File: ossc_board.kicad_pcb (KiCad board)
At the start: 2 copper layers, 124.6 x 68.7 mm, 230 parts, among them J1 VGA, J2 3XRCA_CONN, J3 SCART-F, J4 HDMI_CONN, J5 5VDC_IN, J6 SJ1-3533NG, J7 SJ1-3533NG, P1 JTAG_CONN, P3 mSD_CONN, Q1 BC847, Q2 BC857, SW1 SPST, SW2 SW_PUSH, SW3 SW_PUSH, SW4 DPDT, U1 TVP7002PZP, U10 S25FL216K, U11 IRM-V538/TR1, U12 TLV70012, U13 TLV70025, U14 TLV70012, U15 TLV70018, U16 TLV70018, U17 THS7353, U2 EP4CE15E22, U3 IT6613, U4 SN74LVC2G17, U5 AP7361C, U6 TLV70033, U7 NCP703SN19T1G, U8 PCM1862, U9 TLV70019, Y1 ACHL-27MHZ-EK, Y2 24.576MHz

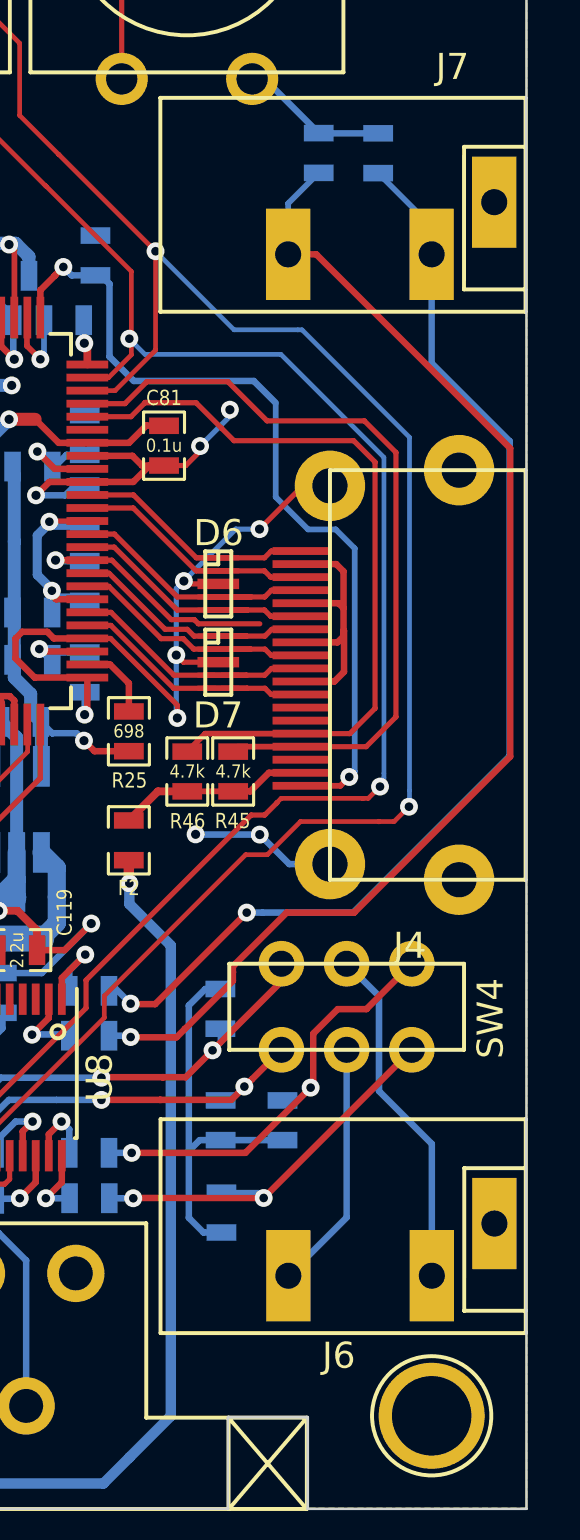
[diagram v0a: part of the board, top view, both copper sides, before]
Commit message: Changed footprint of headphone jack to circular drill
Also, verified DRC rules pass for OSHPark
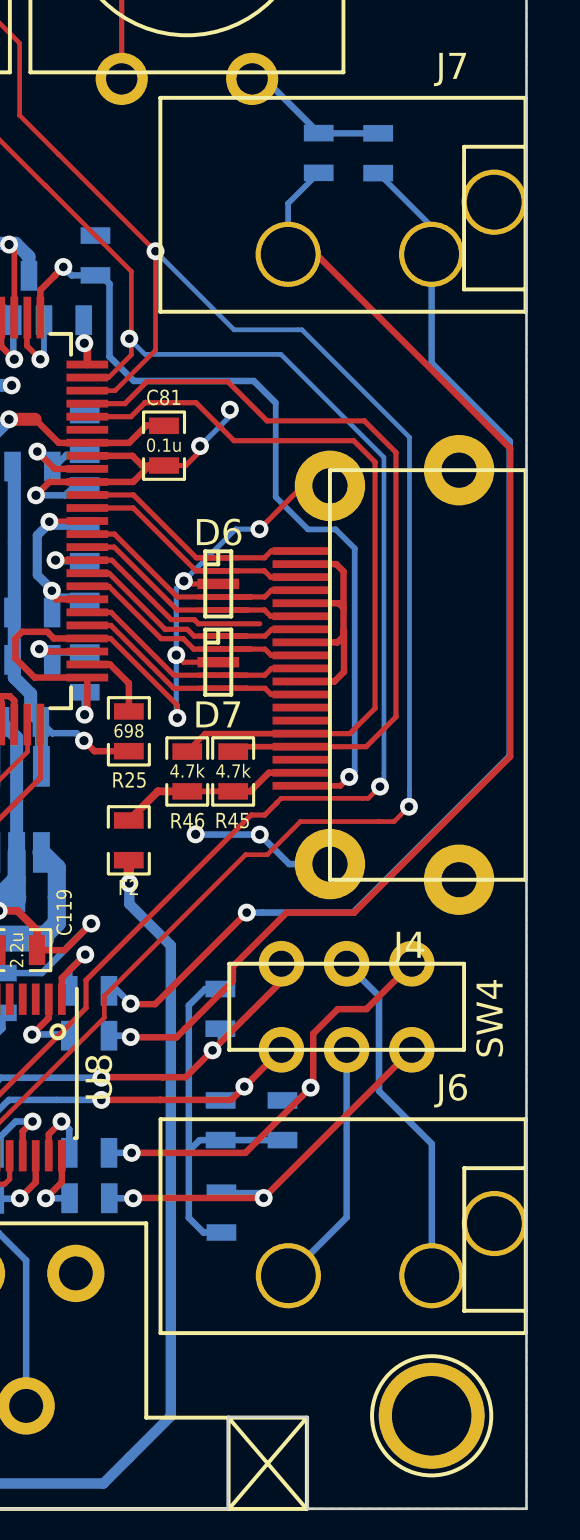
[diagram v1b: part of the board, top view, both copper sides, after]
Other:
- net class Default: clearance 0.16 -> 0.1524; trace_width 0.22 -> 0.1524; via_dia 0.686 -> 0.6858; via_drill 0.33 -> 0.3302
- net class Power: via_drill 0.35 -> 0.3302
- net class digi_hs: via_drill 0.33 -> 0.3302
- rule trace_clearance: 0.16 -> 0.1524
- rule trace_min: 0.16 -> 0.1524
- rule via_min_drill: 0.33 -> 0.3302
- rule via_min_size: 0.686 -> 0.6858
